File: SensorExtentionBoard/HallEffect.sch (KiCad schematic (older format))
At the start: 10 parts

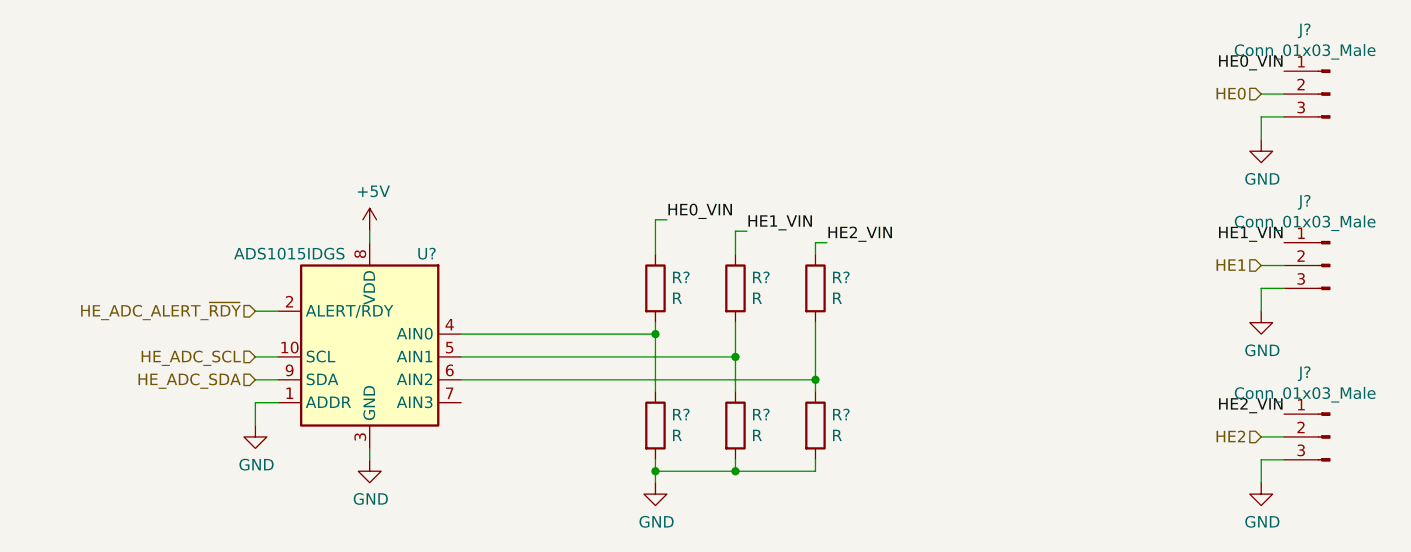
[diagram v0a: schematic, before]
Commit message: Added top level page and made various fixes in other pages of SEB test rig board
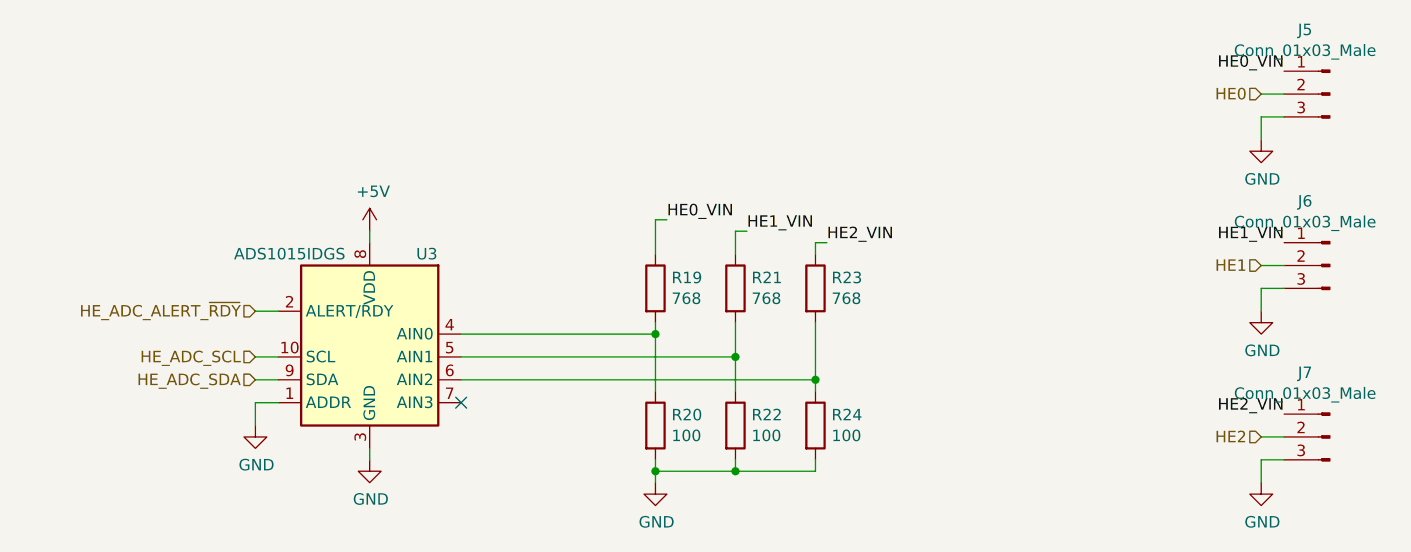
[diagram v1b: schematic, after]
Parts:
- removed R? (x6): R, symbol Device:R
- added R19, R21, R23: 768, Resistor_SMD:R_1206_3216Metric_Pad1.42x1.75mm_HandSolder, symbol Device:R
- added R20, R22, R24: 100, Resistor_SMD:R_1206_3216Metric_Pad1.42x1.75mm_HandSolder, symbol Device:R
- gave numbers to parts that had none: 4
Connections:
- net GND: now also R20.2, R22.2, R24.2
- net HE0_VIN: now also R19.1
- net HE1_VIN: now also R21.1
- net HE2_VIN: now also R23.1
- net at U3.4 (AIN0): now also R19.2, R20.1
- net at U3.5 (AIN1): now also R21.2, R22.1
- net at U3.6 (AIN2): now also R23.2, R24.1
- no-connect marks 0 -> 1
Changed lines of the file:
@@
 $EndDescr
 $Comp
-L Connector:Conn_01x03_Male J?
+L Connector:Conn_01x03_Male J5
 U 1 1 5E39E325
 P 8450 2100
-F 0 "J?" H 8558 2381 50  0000 C CNN
+F 0 "J5" H 8558 2381 50  0000 C CNN
 F 1 "Conn_01x03_Male" H 8558 2290 50  0000 C CNN
 F 2 "" H 8450 2100 50  0001 C CNN
@@
 $EndComp
 $Comp
-L Analog_ADC:ADS1015IDGS U?
+L Analog_ADC:ADS1015IDGS U3
 U 1 1 5E39F012
 P 4250 3250
-F 0 "U?" H 4000 3700 50  0000 C CNN
+F 0 "U3" H 4000 3700 50  0000 C CNN
 F 1 "ADS1015IDGS" H 4600 3700 50  0000 C CNN
 F 2 "Package_SO:TSSOP-10_3x3mm_P0.5mm" H 4250 2750 50  0001 C CNN
@@
 	8150 2100 8250 2100
 $Comp
-L power:GND #PWR?
+L power:GND #PWR018
 U 1 1 5E3A1F0E
 P 8150 2300
-F 0 "#PWR?" H 8150 2050 50  0001 C CNN
+F 0 "#PWR018" H 8150 2050 50  0001 C CNN
 F 1 "GND" H 8155 2127 50  0000 C CNN
 F 2 "" H 8150 2300 50  0001 C CNN
@@
 HE0_VIN
 $Comp
-L Connector:Conn_01x03_Male J?
+L Connector:Conn_01x03_Male J6
 U 1 1 5E3A451B
 P 8450 2850
-F 0 "J?" H 8558 3131 50  0000 C CNN
+F 0 "J6" H 8558 3131 50  0000 C CNN
 F 1 "Conn_01x03_Male" H 8558 3040 50  0000 C CNN
 F 2 "" H 8450 2850 50  0001 C CNN
@@
 	8150 2850 8250 2850
 $Comp
-L power:GND #PWR?
+L power:GND #PWR019
 U 1 1 5E3A4523
 P 8150 3050
-F 0 "#PWR?" H 8150 2800 50  0001 C CNN
+F 0 "#PWR019" H 8150 2800 50  0001 C CNN
 F 1 "GND" H 8155 2877 50  0000 C CNN
 F 2 "" H 8150 3050 50  0001 C CNN
@@
 HE1_VIN
 $Comp
-L Connector:Conn_01x03_Male J?
+L Connector:Conn_01x03_Male J7
 U 1 1 5E3A51E7
 P 8450 3600
-F 0 "J?" H 8558 3881 50  0000 C CNN
+F 0 "J7" H 8558 3881 50  0000 C CNN
 F 1 "Conn_01x03_Male" H 8558 3790 50  0000 C CNN
 F 2 "" H 8450 3600 50  0001 C CNN
@@
 	8150 3600 8250 3600
 $Comp
-L power:GND #PWR?
+L power:GND #PWR020
 U 1 1 5E3A51EF
 P 8150 3800
-F 0 "#PWR?" H 8150 3550 50  0001 C CNN
+F 0 "#PWR020" H 8150 3550 50  0001 C CNN
 F 1 "GND" H 8155 3627 50  0000 C CNN
 F 2 "" H 8150 3800 50  0001 C CNN
@@
 HE2_VIN
 $Comp
-L power:GND #PWR?
+L power:GND #PWR016
 U 1 1 5E3A708B
 P 4250 3700
-F 0 "#PWR?" H 4250 3450 50  0001 C CNN
+F 0 "#PWR016" H 4250 3450 50  0001 C CNN
 F 1 "GND" H 4255 3527 50  0000 C CNN
 F 2 "" H 4250 3700 50  0001 C CNN
@@
 	4250 3700 4250 3650
 $Comp
-L power:GND #PWR?
+L power:GND #PWR014
 U 1 1 5E3A756C
 P 3750 3550
-F 0 "#PWR?" H 3750 3300 50  0001 C CNN
+F 0 "#PWR014" H 3750 3300 50  0001 C CNN
 F 1 "GND" H 3755 3377 50  0000 C CNN
 F 2 "" H 3750 3550 50  0001 C CNN
@@
 Wire Wire Line
 	3750 3350 3850 3350
-$Comp
-L Device:R R?
-U 1 1 5E3AE546
-P 5500 2950
-F 0 "R?" H 5570 2996 50  0000 L CNN
-F 1 "R" H 5570 2905 50  0000 L CNN
-F 2 "" V 5430 2950 50  0001 C CNN
-F 3 "~" H 5500 2950 50  0001 C CNN
-	1    5500 2950
-	1    0    0    -1
-$EndComp
-$Comp
-L Device:R R?
-U 1 1 5E3AEA93
-P 5500 3550
-F 0 "R?" H 5570 3596 50  0000 L CNN
-F 1 "R" H 5570 3505 50  0000 L CNN
-F 2 "" V 5430 3550 50  0001 C CNN
-F 3 "~" H 5500 3550 50  0001 C CNN
-	1    5500 3550
-	1    0    0    -1
-$EndComp
 Wire Wire Line
 	4650 3150 5500 3150
-$Comp
-L Device:R R?
-U 1 1 5E3B0757
-P 5850 2950
-F 0 "R?" H 5920 2996 50  0000 L CNN
-F 1 "R" H 5920 2905 50  0000 L CNN
-F 2 "" V 5780 2950 50  0001 C CNN
-F 3 "~" H 5850 2950 50  0001 C CNN
-	1    5850 2950
-	1    0    0    -1
-$EndComp
-$Comp
-L Device:R R?
-U 1 1 5E3B0AAE
-P 5850 3550
-F 0 "R?" H 5920 3596 50  0000 L CNN
-F 1 "R" H 5920 3505 50  0000 L CNN
-F 2 "" V 5780 3550 50  0001 C CNN
-F 3 "~" H 5850 3550 50  0001 C CNN
-	1    5850 3550
-	1    0    0    -1
-$EndComp
-$Comp
-L Device:R R?
-U 1 1 5E3B0DC2
-P 6200 3550
-F 0 "R?" H 6270 3596 50  0000 L CNN
-F 1 "R" H 6270 3505 50  0000 L CNN
-F 2 "" V 6130 3550 50  0001 C CNN
-F 3 "~" H 6200 3550 50  0001 C CNN
-	1    6200 3550
-	1    0    0    -1
-$EndComp
-$Comp
-L Device:R R?
-U 1 1 5E3B1055
-P 6200 2950
-F 0 "R?" H 6270 2996 50  0000 L CNN
-F 1 "R" H 6270 2905 50  0000 L CNN
-F 2 "" V 6130 2950 50  0001 C CNN
-F 3 "~" H 6200 2950 50  0001 C CNN
-	1    6200 2950
-	1    0    0    -1
-$EndComp
 Wire Wire Line
 	4650 3250 5850 3250
@@
 Connection ~ 6200 3350
 $Comp
-L power:GND #PWR?
+L power:GND #PWR017
 U 1 1 5E3B85EB
 P 5500 3800
-F 0 "#PWR?" H 5500 3550 50  0001 C CNN
+F 0 "#PWR017" H 5500 3550 50  0001 C CNN
 F 1 "GND" H 5505 3627 50  0000 C CNN
 F 2 "" H 5500 3800 50  0001 C CNN
@@
 	5500 2650 5500 2800
 $Comp
-L power:+5V #PWR?
+L power:+5V #PWR015
 U 1 1 5E3C2F7A
 P 4250 2700
-F 0 "#PWR?" H 4250 2550 50  0001 C CNN
+F 0 "#PWR015" H 4250 2550 50  0001 C CNN
 F 1 "+5V" H 4265 2873 50  0000 C CNN
 F 2 "" H 4250 2700 50  0001 C CNN
@@
 Wire Wire Line
 	4250 2700 4250 2750
+NoConn ~ 4650 3450
+$Comp
+L Device:R R?
+U 1 1 5E628041
+P 5500 3550
+AR Path="/5E628041" Ref="R?"  Part="1"
+AR Path="/5E059E7A/5E628041" Ref="R20"  Part="1"
+F 0 "R20" H 5570 3596 50  0000 L CNN
+F 1 "100" H 5570 3505 50  0000 L CNN
+F 2 "Resistor_SMD:R_1206_3216Metric_Pad1.42x1.75mm_HandSolder" V 5430 3550 50  0001 C CNN
+F 3 "~" H 5500 3550 50  0001 C CNN
+	1    5500 3550
+	1    0    0    -1
+$EndComp
+$Comp
+L Device:R R?
+U 1 1 5E63C1A6
+P 6200 2950
+AR Path="/5E059EAC/5E63C1A6" Ref="R?"  Part="1"
+AR Path="/5E059E7A/5E63C1A6" Ref="R23"  Part="1"
+F 0 "R23" H 6270 2996 50  0000 L CNN
+F 1 "768" H 6270 2905 50  0000 L CNN
+F 2 "Resistor_SMD:R_1206_3216Metric_Pad1.42x1.75mm_HandSolder" V 6130 2950 50  0001 C CNN
+F 3 "~" H 6200 2950 50  0001 C CNN
+	1    6200 2950
+	1    0    0    -1
+$EndComp
+$Comp
+L Device:R R?
+U 1 1 5E63F6B5
+P 5850 2950
+AR Path="/5E059EAC/5E63F6B5" Ref="R?"  Part="1"
+AR Path="/5E059E7A/5E63F6B5" Ref="R21"  Part="1"
+F 0 "R21" H 5920 2996 50  0000 L CNN
+F 1 "768" H 5920 2905 50  0000 L CNN
+F 2 "Resistor_SMD:R_1206_3216Metric_Pad1.42x1.75mm_HandSolder" V 5780 2950 50  0001 C CNN
+F 3 "~" H 5850 2950 50  0001 C CNN
+	1    5850 2950
+	1    0    0    -1
+$EndComp
+$Comp
+L Device:R R?
+U 1 1 5E63FA92
+P 5500 2950
+AR Path="/5E059EAC/5E63FA92" Ref="R?"  Part="1"
+AR Path="/5E059E7A/5E63FA92" Ref="R19"  Part="1"
+F 0 "R19" H 5570 2996 50  0000 L CNN
+F 1 "768" H 5570 2905 50  0000 L CNN
+F 2 "Resistor_SMD:R_1206_3216Metric_Pad1.42x1.75mm_HandSolder" V 5430 2950 50  0001 C CNN
+F 3 "~" H 5500 2950 50  0001 C CNN
+	1    5500 2950
+	1    0    0    -1
+$EndComp
+$Comp
+L Device:R R?
+U 1 1 5E6458A4
+P 5850 3550
+AR Path="/5E6458A4" Ref="R?"  Part="1"
+AR Path="/5E059E7A/5E6458A4" Ref="R22"  Part="1"
+F 0 "R22" H 5920 3596 50  0000 L CNN
+F 1 "100" H 5920 3505 50  0000 L CNN
+F 2 "Resistor_SMD:R_1206_3216Metric_Pad1.42x1.75mm_HandSolder" V 5780 3550 50  0001 C CNN
+F 3 "~" H 5850 3550 50  0001 C CNN
+	1    5850 3550
+	1    0    0    -1
+$EndComp
+$Comp
+L Device:R R?
+U 1 1 5E645AA9
+P 6200 3550
+AR Path="/5E645AA9" Ref="R?"  Part="1"
+AR Path="/5E059E7A/5E645AA9" Ref="R24"  Part="1"
+F 0 "R24" H 6270 3596 50  0000 L CNN
+F 1 "100" H 6270 3505 50  0000 L CNN
+F 2 "Resistor_SMD:R_1206_3216Metric_Pad1.42x1.75mm_HandSolder" V 6130 3550 50  0001 C CNN
+F 3 "~" H 6200 3550 50  0001 C CNN
+	1    6200 3550
+	1    0    0    -1
+$EndComp
 $EndSCHEMATC

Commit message: Moved some stuff and added footprints to components
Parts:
- J5, J6, J7: footprint (none) -> Connector_Molex:Molex_MicroClasp_55932-0310_1x03_P2.00mm_Vertical
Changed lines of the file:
@@
 F 0 "J5" H 8558 2381 50  0000 C CNN
 F 1 "Conn_01x03_Male" H 8558 2290 50  0000 C CNN
-F 2 "" H 8450 2100 50  0001 C CNN
+F 2 "Connector_Molex:Molex_MicroClasp_55932-0310_1x03_P2.00mm_Vertical" H 8450 2100 50  0001 C CNN
 F 3 "~" H 8450 2100 50  0001 C CNN
 	1    8450 2100
@@
 F 0 "J6" H 8558 3131 50  0000 C CNN
 F 1 "Conn_01x03_Male" H 8558 3040 50  0000 C CNN
-F 2 "" H 8450 2850 50  0001 C CNN
+F 2 "Connector_Molex:Molex_MicroClasp_55932-0310_1x03_P2.00mm_Vertical" H 8450 2850 50  0001 C CNN
 F 3 "~" H 8450 2850 50  0001 C CNN
 	1    8450 2850
@@
 F 0 "J7" H 8558 3881 50  0000 C CNN
 F 1 "Conn_01x03_Male" H 8558 3790 50  0000 C CNN
-F 2 "" H 8450 3600 50  0001 C CNN
+F 2 "Connector_Molex:Molex_MicroClasp_55932-0310_1x03_P2.00mm_Vertical" H 8450 3600 50  0001 C CNN
 F 3 "~" H 8450 3600 50  0001 C CNN
 	1    8450 3600

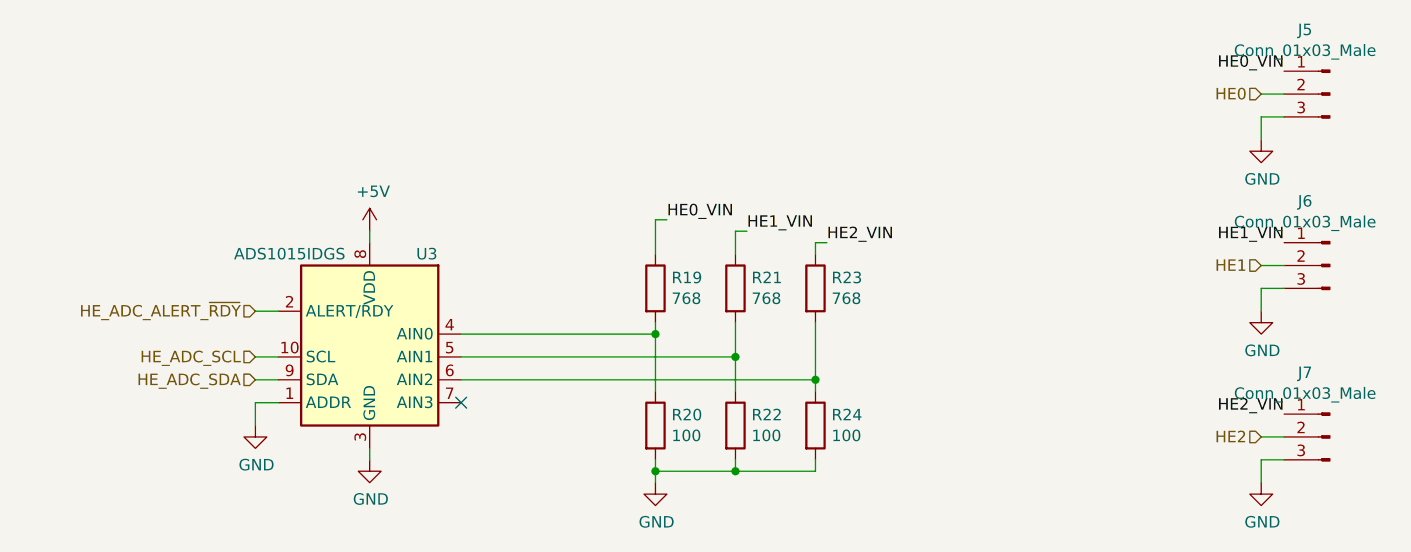
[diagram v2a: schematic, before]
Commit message: Added decoupling caps
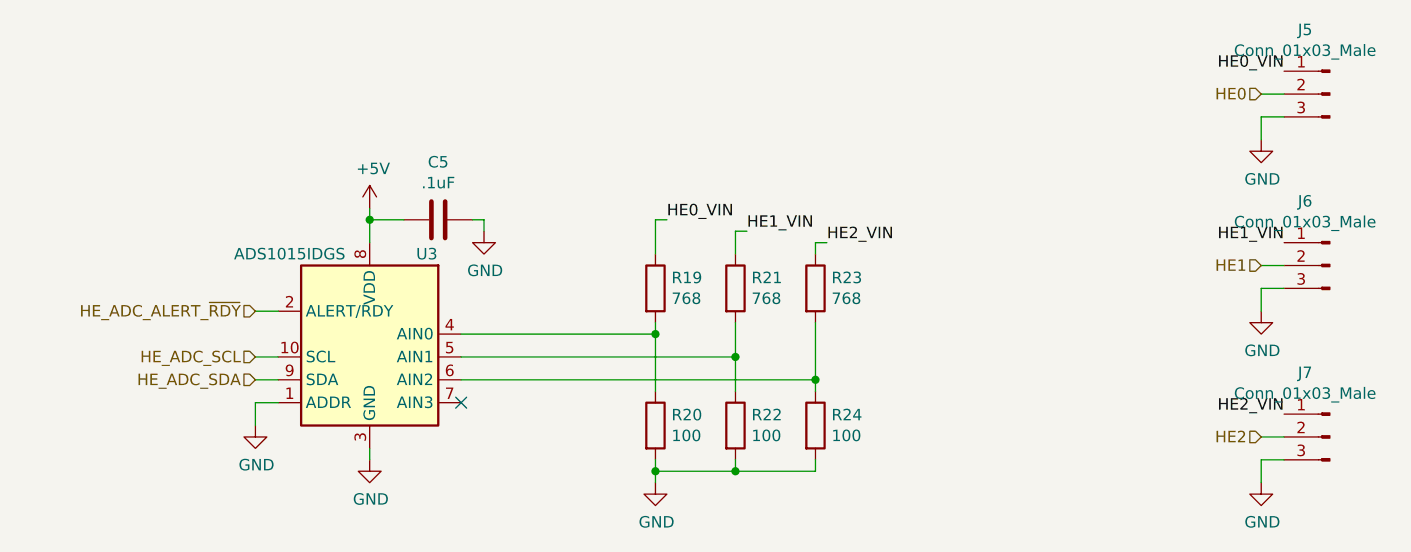
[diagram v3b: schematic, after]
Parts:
- added C5: .1uF, symbol Device:C
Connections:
- net +5V: now also C5.2
- net GND: now also C5.1
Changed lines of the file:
@@
 	8150 2100 8250 2100
 $Comp
-L power:GND #PWR018
+L power:GND #PWR021
 U 1 1 5E3A1F0E
 P 8150 2300
-F 0 "#PWR018" H 8150 2050 50  0001 C CNN
+F 0 "#PWR021" H 8150 2050 50  0001 C CNN
 F 1 "GND" H 8155 2127 50  0000 C CNN
 F 2 "" H 8150 2300 50  0001 C CNN
@@
 	8150 2850 8250 2850
 $Comp
-L power:GND #PWR019
+L power:GND #PWR022
 U 1 1 5E3A4523
 P 8150 3050
-F 0 "#PWR019" H 8150 2800 50  0001 C CNN
+F 0 "#PWR022" H 8150 2800 50  0001 C CNN
 F 1 "GND" H 8155 2877 50  0000 C CNN
 F 2 "" H 8150 3050 50  0001 C CNN
@@
 	8150 3600 8250 3600
 $Comp
-L power:GND #PWR020
+L power:GND #PWR023
 U 1 1 5E3A51EF
 P 8150 3800
-F 0 "#PWR020" H 8150 3550 50  0001 C CNN
+F 0 "#PWR023" H 8150 3550 50  0001 C CNN
 F 1 "GND" H 8155 3627 50  0000 C CNN
 F 2 "" H 8150 3800 50  0001 C CNN
@@
 HE2_VIN
 $Comp
-L power:GND #PWR016
+L power:GND #PWR018
 U 1 1 5E3A708B
 P 4250 3700
-F 0 "#PWR016" H 4250 3450 50  0001 C CNN
+F 0 "#PWR018" H 4250 3450 50  0001 C CNN
 F 1 "GND" H 4255 3527 50  0000 C CNN
 F 2 "" H 4250 3700 50  0001 C CNN
@@
 	4250 3700 4250 3650
 $Comp
-L power:GND #PWR014
+L power:GND #PWR016
 U 1 1 5E3A756C
 P 3750 3550
-F 0 "#PWR014" H 3750 3300 50  0001 C CNN
+F 0 "#PWR016" H 3750 3300 50  0001 C CNN
 F 1 "GND" H 3755 3377 50  0000 C CNN
 F 2 "" H 3750 3550 50  0001 C CNN
@@
 Connection ~ 6200 3350
 $Comp
-L power:GND #PWR017
+L power:GND #PWR020
 U 1 1 5E3B85EB
 P 5500 3800
-F 0 "#PWR017" H 5500 3550 50  0001 C CNN
+F 0 "#PWR020" H 5500 3550 50  0001 C CNN
 F 1 "GND" H 5505 3627 50  0000 C CNN
 F 2 "" H 5500 3800 50  0001 C CNN
@@
 	5500 2650 5500 2800
 $Comp
-L power:+5V #PWR015
+L power:+5V #PWR017
 U 1 1 5E3C2F7A
-P 4250 2700
-F 0 "#PWR015" H 4250 2550 50  0001 C CNN
-F 1 "+5V" H 4265 2873 50  0000 C CNN
-F 2 "" H 4250 2700 50  0001 C CNN
-F 3 "" H 4250 2700 50  0001 C CNN
-	1    4250 2700
-	1    0    0    -1
-$EndComp
-Wire Wire Line
-	4250 2700 4250 2750
+P 4250 2600
+F 0 "#PWR017" H 4250 2450 50  0001 C CNN
+F 1 "+5V" H 4265 2773 50  0000 C CNN
+F 2 "" H 4250 2600 50  0001 C CNN
+F 3 "" H 4250 2600 50  0001 C CNN
+	1    4250 2600
+	1    0    0    -1
+$EndComp
+Wire Wire Line
+	4250 2600 4250 2650
 NoConn ~ 4650 3450
 $Comp
@@
 	1    0    0    -1
 $EndComp
+$Comp
+L Device:C C?
+U 1 1 5E24F640
+P 4550 2650
+AR Path="/5E24F640" Ref="C?"  Part="1"
+AR Path="/5E059E7A/5E24F640" Ref="C5"  Part="1"
+F 0 "C5" V 4298 2650 50  0000 C CNN
+F 1 ".1uF" V 4389 2650 50  0000 C CNN
+F 2 "" H 4588 2500 50  0001 C CNN
+F 3 "~" H 4550 2650 50  0001 C CNN
+	1    4550 2650
+	0    1    1    0
+$EndComp
+$Comp
+L power:GND #PWR?
+U 1 1 5E24F646
+P 4750 2700
+AR Path="/5E24F646" Ref="#PWR?"  Part="1"
+AR Path="/5E059E7A/5E24F646" Ref="#PWR019"  Part="1"
+F 0 "#PWR019" H 4750 2450 50  0001 C CNN
+F 1 "GND" H 4755 2527 50  0000 C CNN
+F 2 "" H 4750 2700 50  0001 C CNN
+F 3 "" H 4750 2700 50  0001 C CNN
+	1    4750 2700
+	1    0    0    -1
+$EndComp
+Wire Wire Line
+	4700 2650 4750 2650
+Wire Wire Line
+	4750 2650 4750 2700
+Wire Wire Line
+	4400 2650 4250 2650
+Connection ~ 4250 2650
+Wire Wire Line
+	4250 2650 4250 2750
 $EndSCHEMATC
